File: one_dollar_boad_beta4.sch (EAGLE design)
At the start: 38 parts, among them IC1 ATTINY85, X1 USBPCB

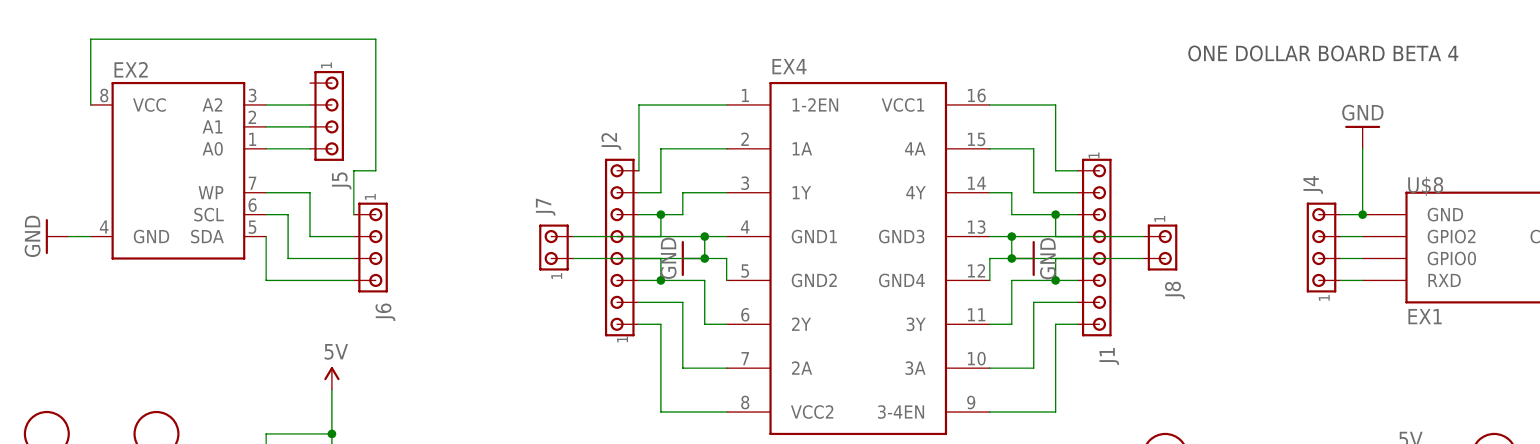
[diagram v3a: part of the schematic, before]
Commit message: GND retirado
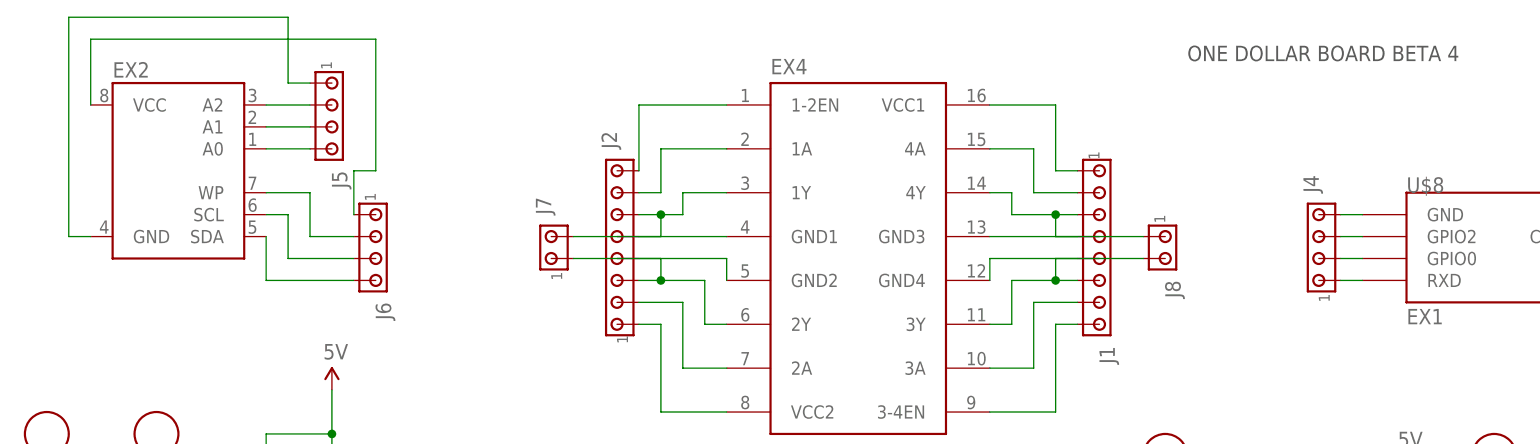
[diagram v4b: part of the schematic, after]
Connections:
- new net N$22: J4.4, U$8.GND
- new net N$49: EX4.GND2, J2.4
- new net N$50: EX4.GND1, J2.5
- new net N$51: EX4.GND4, J1.5
- new net N$52: EX4.GND3, J1.4
- new net N$53: EX2.GND, J5.1
- net GND: no longer EX2.GND, EX4.GND1, EX4.GND2, EX4.GND3, EX4.GND4, J1.4, J1.5, J2.4, J2.5, J4.4, U$8.GND
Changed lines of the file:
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@@
 <?xml version="1.0" encoding="utf-8"?>
 <!DOCTYPE eagle SYSTEM "eagle.dtd">
-<eagle version="6.6.0">
+<eagle version="7.5.0">
 <drawing>
 <settings>
@@
 <part name="J4" library="con-amp" deviceset="MTA04-100" device=""/>
 <part name="EX2" library="atmel" deviceset="AT24C*" device="P" value=""/>
-<part name="GND8" library="supply1" deviceset="GND" device=""/>
-<part name="GND9" library="SparkFun" deviceset="GND" device=""/>
-<part name="GND10" library="SparkFun" deviceset="GND" device=""/>
-<part name="GND11" library="SparkFun" deviceset="GND" device=""/>
 <part name="J5" library="con-amp" deviceset="MTA04-100" device=""/>
 <part name="J6" library="con-amp" deviceset="MTA04-100" device=""/>
@@
 <instance part="J4" gate="G$1" x="93.98" y="93.98" rot="R90"/>
 <instance part="EX2" gate="G$1" x="-38.1" y="104.14"/>
-<instance part="GND8" gate="1" x="-53.34" y="96.52" rot="R270"/>
-<instance part="GND9" gate="1" x="99.06" y="109.22" rot="R180"/>
-<instance part="GND10" gate="1" x="60.96" y="93.98" rot="R90"/>
-<instance part="GND11" gate="1" x="20.32" y="93.98" rot="R270"/>
 <instance part="J5" gate="G$1" x="-20.32" y="111.76" rot="R270"/>
 <instance part="J6" gate="G$1" x="-15.24" y="96.52" rot="R270"/>
@@
 </segment>
 <segment>
-<pinref part="EX2" gate="G$1" pin="GND"/>
-<pinref part="GND8" gate="1" pin="GND"/>
-<wire x1="-48.26" y1="96.52" x2="-50.8" y2="96.52" width="0.1524" layer="91"/>
-</segment>
-<segment>
-<pinref part="GND10" gate="1" pin="GND"/>
-<wire x1="58.42" y1="96.52" x2="58.42" y2="93.98" width="0.1524" layer="91"/>
-<pinref part="EX4" gate="G$1" pin="GND4"/>
-<wire x1="58.42" y1="93.98" x2="55.88" y2="93.98" width="0.1524" layer="91"/>
-<wire x1="55.88" y1="93.98" x2="55.88" y2="91.44" width="0.1524" layer="91"/>
-<pinref part="EX4" gate="G$1" pin="GND3"/>
-<wire x1="58.42" y1="96.52" x2="55.88" y2="96.52" width="0.1524" layer="91"/>
-<junction x="58.42" y="93.98"/>
-<pinref part="J1" gate="G$1" pin="4"/>
-<wire x1="66.04" y1="96.52" x2="58.42" y2="96.52" width="0.1524" layer="91"/>
-<pinref part="J1" gate="G$1" pin="5"/>
-<wire x1="66.04" y1="93.98" x2="58.42" y2="93.98" width="0.1524" layer="91"/>
-<junction x="58.42" y="96.52"/>
-</segment>
-<segment>
-<pinref part="EX4" gate="G$1" pin="GND1"/>
-<pinref part="GND11" gate="1" pin="GND"/>
-<wire x1="25.4" y1="96.52" x2="22.86" y2="96.52" width="0.1524" layer="91"/>
-<wire x1="22.86" y1="96.52" x2="22.86" y2="93.98" width="0.1524" layer="91"/>
-<pinref part="EX4" gate="G$1" pin="GND2"/>
-<wire x1="25.4" y1="91.44" x2="25.4" y2="93.98" width="0.1524" layer="91"/>
-<wire x1="25.4" y1="93.98" x2="22.86" y2="93.98" width="0.1524" layer="91"/>
-<junction x="22.86" y="93.98"/>
-<pinref part="J2" gate="G$1" pin="5"/>
-<wire x1="15.24" y1="96.52" x2="22.86" y2="96.52" width="0.1524" layer="91"/>
-<pinref part="J2" gate="G$1" pin="4"/>
-<wire x1="15.24" y1="93.98" x2="22.86" y2="93.98" width="0.1524" layer="91"/>
-<junction x="22.86" y="96.52"/>
-</segment>
-<segment>
-<pinref part="U$8" gate="G$1" pin="GND"/>
-<pinref part="GND9" gate="1" pin="GND"/>
-<wire x1="99.06" y1="99.06" x2="99.06" y2="106.68" width="0.1524" layer="91"/>
-<pinref part="J4" gate="G$1" pin="4"/>
-<wire x1="96.52" y1="99.06" x2="99.06" y2="99.06" width="0.1524" layer="91"/>
-<junction x="99.06" y="99.06"/>
-</segment>
-<segment>
 <pinref part="GND4" gate="1" pin="GND"/>
 <wire x1="116.84" y1="50.8" x2="116.84" y2="48.26" width="0.1524" layer="91"/>
@@
 </segment>
 </net>
+<net name="N$22" class="0">
+<segment>
+<pinref part="U$8" gate="G$1" pin="GND"/>
+<pinref part="J4" gate="G$1" pin="4"/>
+<wire x1="96.52" y1="99.06" x2="99.06" y2="99.06" width="0.1524" layer="91"/>
+</segment>
+</net>
+<net name="N$49" class="0">
+<segment>
+<pinref part="EX4" gate="G$1" pin="GND2"/>
+<wire x1="25.4" y1="91.44" x2="25.4" y2="93.98" width="0.1524" layer="91"/>
+<pinref part="J2" gate="G$1" pin="4"/>
+<wire x1="15.24" y1="93.98" x2="25.4" y2="93.98" width="0.1524" layer="91"/>
+</segment>
+</net>
+<net name="N$50" class="0">
+<segment>
+<pinref part="EX4" gate="G$1" pin="GND1"/>
+<pinref part="J2" gate="G$1" pin="5"/>
+<wire x1="15.24" y1="96.52" x2="25.4" y2="96.52" width="0.1524" layer="91"/>
+</segment>
+</net>
+<net name="N$51" class="0">
+<segment>
+<pinref part="EX4" gate="G$1" pin="GND4"/>
+<wire x1="55.88" y1="93.98" x2="55.88" y2="91.44" width="0.1524" layer="91"/>
+<pinref part="J1" gate="G$1" pin="5"/>
+<wire x1="66.04" y1="93.98" x2="55.88" y2="93.98" width="0.1524" layer="91"/>
+</segment>
+</net>
+<net name="N$52" class="0">
+<segment>
+<pinref part="EX4" gate="G$1" pin="GND3"/>
+<pinref part="J1" gate="G$1" pin="4"/>
+<wire x1="66.04" y1="96.52" x2="55.88" y2="96.52" width="0.1524" layer="91"/>
+</segment>
+</net>
+<net name="N$53" class="0">
+<segment>
+<pinref part="EX2" gate="G$1" pin="GND"/>
+<wire x1="-48.26" y1="96.52" x2="-50.8" y2="96.52" width="0.1524" layer="91"/>
+<wire x1="-50.8" y1="96.52" x2="-50.8" y2="121.92" width="0.1524" layer="91"/>
+<wire x1="-50.8" y1="121.92" x2="-25.4" y2="121.92" width="0.1524" layer="91"/>
+<wire x1="-25.4" y1="121.92" x2="-25.4" y2="114.3" width="0.1524" layer="91"/>
+<pinref part="J5" gate="G$1" pin="1"/>
+<wire x1="-25.4" y1="114.3" x2="-22.86" y2="114.3" width="0.1524" layer="91"/>
+</segment>
+</net>

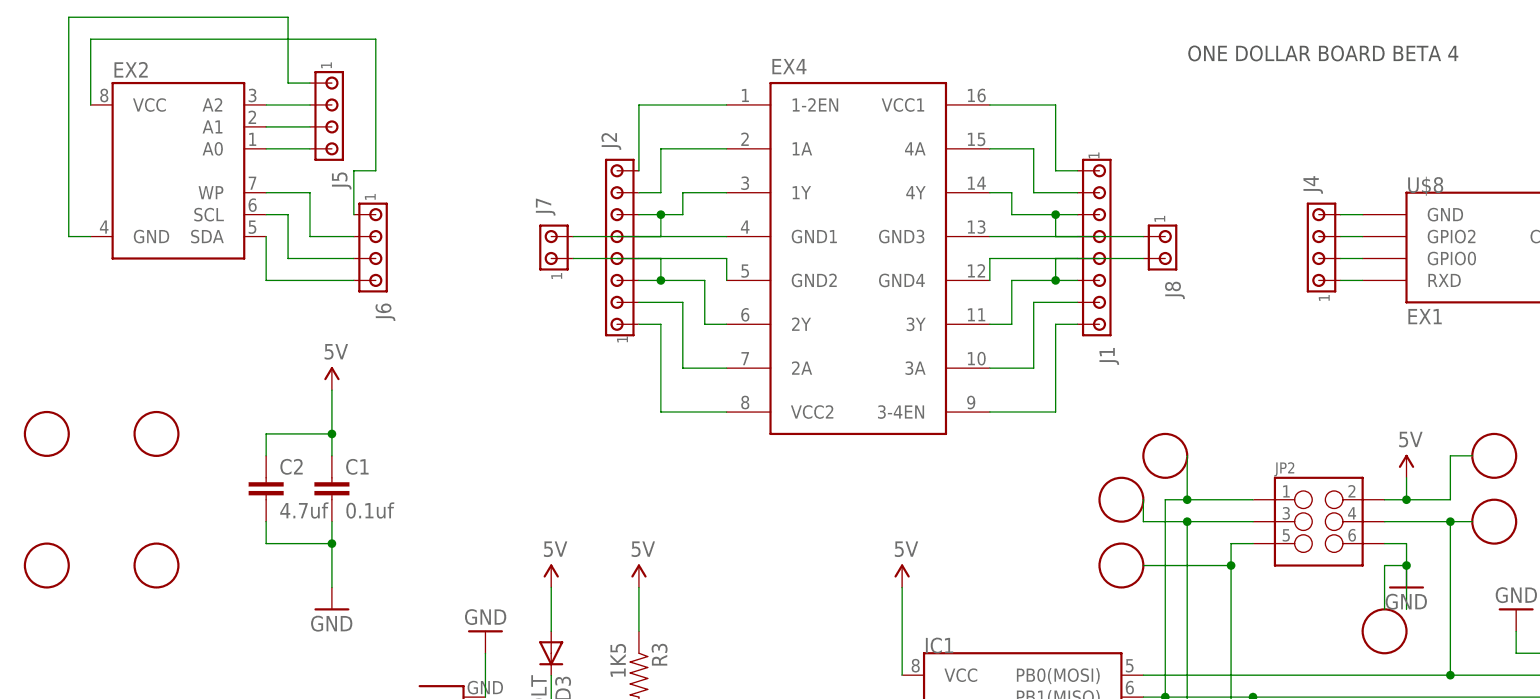
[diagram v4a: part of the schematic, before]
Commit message: Added files via upload
Adicionado alimentação externa
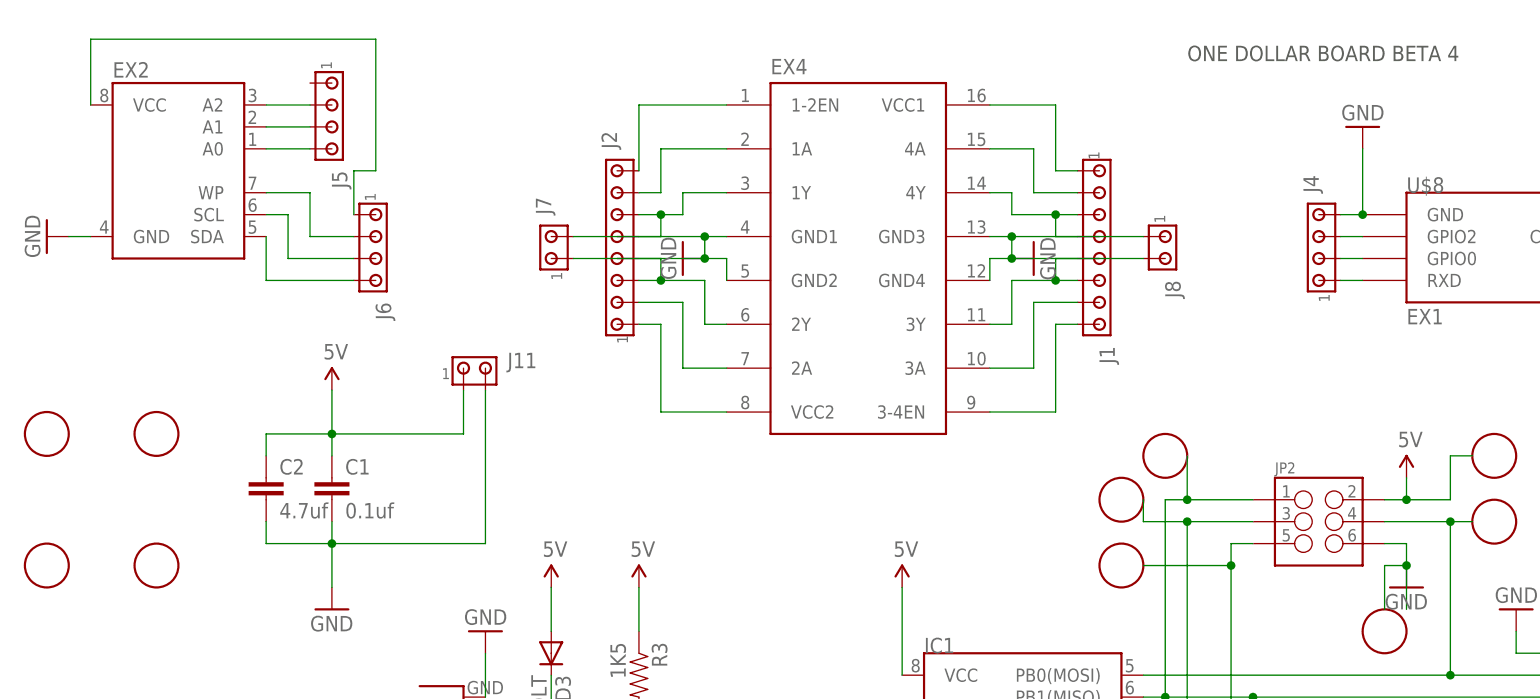
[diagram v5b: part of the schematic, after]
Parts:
- added J11: (no value), con-amp:MTA02-100
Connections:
- removed net N$22: J4.4, U$8.GND
- removed net N$49: EX4.GND2, J2.4
- removed net N$50: EX4.GND1, J2.5
- removed net N$51: EX4.GND4, J1.5
- removed net N$52: EX4.GND3, J1.4
- removed net N$53: EX2.GND, J5.1
- net 5V: now also J11.1
- net GND: now also EX2.GND, EX4.GND1, EX4.GND2, EX4.GND3, EX4.GND4, J1.4, J1.5, J11.2, J2.4, J2.5, J4.4, U$8.GND
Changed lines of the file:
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@@
 <?xml version="1.0" encoding="utf-8"?>
 <!DOCTYPE eagle SYSTEM "eagle.dtd">
-<eagle version="7.5.0">
+<eagle version="7.2.0">
 <drawing>
 <settings>
@@
 <part name="J4" library="con-amp" deviceset="MTA04-100" device=""/>
 <part name="EX2" library="atmel" deviceset="AT24C*" device="P" value=""/>
+<part name="GND8" library="supply1" deviceset="GND" device=""/>
+<part name="GND9" library="SparkFun" deviceset="GND" device=""/>
+<part name="GND10" library="SparkFun" deviceset="GND" device=""/>
+<part name="GND11" library="SparkFun" deviceset="GND" device=""/>
 <part name="J5" library="con-amp" deviceset="MTA04-100" device=""/>
 <part name="J6" library="con-amp" deviceset="MTA04-100" device=""/>
@@
 <part name="J9" library="con-amp" deviceset="MTA03-100" device=""/>
 <part name="J10" library="con-amp" deviceset="MTA03-100" device=""/>
+<part name="J11" library="con-amp" deviceset="MTA02-100" device=""/>
 </parts>
 <sheets>
@@
 <instance part="J4" gate="G$1" x="93.98" y="93.98" rot="R90"/>
 <instance part="EX2" gate="G$1" x="-38.1" y="104.14"/>
+<instance part="GND8" gate="1" x="-53.34" y="96.52" rot="R270"/>
+<instance part="GND9" gate="1" x="99.06" y="109.22" rot="R180"/>
+<instance part="GND10" gate="1" x="60.96" y="93.98" rot="R90"/>
+<instance part="GND11" gate="1" x="20.32" y="93.98" rot="R270"/>
 <instance part="J5" gate="G$1" x="-20.32" y="111.76" rot="R270"/>
 <instance part="J6" gate="G$1" x="-15.24" y="96.52" rot="R270"/>
@@
 <instance part="J9" gate="G$1" x="132.08" y="76.2"/>
 <instance part="J10" gate="G$1" x="132.08" y="68.58" rot="R180"/>
+<instance part="J11" gate="G$1" x="-5.08" y="81.28"/>
 </instances>
 <busses>
@@
 <wire x1="-27.94" y1="60.96" x2="-27.94" y2="63.5" width="0.1524" layer="91"/>
 <junction x="-20.32" y="60.96"/>
+<pinref part="J11" gate="G$1" pin="2"/>
+<wire x1="-2.54" y1="78.74" x2="-2.54" y2="60.96" width="0.1524" layer="91"/>
+<wire x1="-2.54" y1="60.96" x2="-20.32" y2="60.96" width="0.1524" layer="91"/>
 </segment>
 <segment>
@@
 <pinref part="GND7" gate="1" pin="GND"/>
 <wire x1="99.06" y1="5.08" x2="111.76" y2="5.08" width="0.1524" layer="91"/>
+</segment>
+<segment>
+<pinref part="EX2" gate="G$1" pin="GND"/>
+<pinref part="GND8" gate="1" pin="GND"/>
+<wire x1="-48.26" y1="96.52" x2="-50.8" y2="96.52" width="0.1524" layer="91"/>
+</segment>
+<segment>
+<pinref part="GND10" gate="1" pin="GND"/>
+<wire x1="58.42" y1="96.52" x2="58.42" y2="93.98" width="0.1524" layer="91"/>
+<pinref part="EX4" gate="G$1" pin="GND4"/>
+<wire x1="58.42" y1="93.98" x2="55.88" y2="93.98" width="0.1524" layer="91"/>
+<wire x1="55.88" y1="93.98" x2="55.88" y2="91.44" width="0.1524" layer="91"/>
+<pinref part="EX4" gate="G$1" pin="GND3"/>
+<wire x1="58.42" y1="96.52" x2="55.88" y2="96.52" width="0.1524" layer="91"/>
+<junction x="58.42" y="93.98"/>
+<pinref part="J1" gate="G$1" pin="4"/>
+<wire x1="66.04" y1="96.52" x2="58.42" y2="96.52" width="0.1524" layer="91"/>
+<pinref part="J1" gate="G$1" pin="5"/>
+<wire x1="66.04" y1="93.98" x2="58.42" y2="93.98" width="0.1524" layer="91"/>
+<junction x="58.42" y="96.52"/>
+</segment>
+<segment>
+<pinref part="EX4" gate="G$1" pin="GND1"/>
+<pinref part="GND11" gate="1" pin="GND"/>
+<wire x1="25.4" y1="96.52" x2="22.86" y2="96.52" width="0.1524" layer="91"/>
+<wire x1="22.86" y1="96.52" x2="22.86" y2="93.98" width="0.1524" layer="91"/>
+<pinref part="EX4" gate="G$1" pin="GND2"/>
+<wire x1="25.4" y1="91.44" x2="25.4" y2="93.98" width="0.1524" layer="91"/>
+<wire x1="25.4" y1="93.98" x2="22.86" y2="93.98" width="0.1524" layer="91"/>
+<junction x="22.86" y="93.98"/>
+<pinref part="J2" gate="G$1" pin="5"/>
+<wire x1="15.24" y1="96.52" x2="22.86" y2="96.52" width="0.1524" layer="91"/>
+<pinref part="J2" gate="G$1" pin="4"/>
+<wire x1="15.24" y1="93.98" x2="22.86" y2="93.98" width="0.1524" layer="91"/>
+<junction x="22.86" y="96.52"/>
+</segment>
+<segment>
+<pinref part="U$8" gate="G$1" pin="GND"/>
+<pinref part="GND9" gate="1" pin="GND"/>
+<wire x1="99.06" y1="99.06" x2="99.06" y2="106.68" width="0.1524" layer="91"/>
+<pinref part="J4" gate="G$1" pin="4"/>
+<wire x1="96.52" y1="99.06" x2="99.06" y2="99.06" width="0.1524" layer="91"/>
+<junction x="99.06" y="99.06"/>
 </segment>
 <segment>
@@
 <wire x1="-27.94" y1="73.66" x2="-20.32" y2="73.66" width="0.1524" layer="91"/>
 <junction x="-20.32" y="73.66"/>
+<pinref part="J11" gate="G$1" pin="1"/>
+<wire x1="-5.08" y1="78.74" x2="-5.08" y2="73.66" width="0.1524" layer="91"/>
+<wire x1="-5.08" y1="73.66" x2="-20.32" y2="73.66" width="0.1524" layer="91"/>
 </segment>
 <segment>
@@
 </segment>
 </net>
-<net name="N$22" class="0">
-<segment>
-<pinref part="U$8" gate="G$1" pin="GND"/>
-<pinref part="J4" gate="G$1" pin="4"/>
-<wire x1="96.52" y1="99.06" x2="99.06" y2="99.06" width="0.1524" layer="91"/>
-</segment>
-</net>
-<net name="N$49" class="0">
-<segment>
-<pinref part="EX4" gate="G$1" pin="GND2"/>
-<wire x1="25.4" y1="91.44" x2="25.4" y2="93.98" width="0.1524" layer="91"/>
-<pinref part="J2" gate="G$1" pin="4"/>
-<wire x1="15.24" y1="93.98" x2="25.4" y2="93.98" width="0.1524" layer="91"/>
-</segment>
-</net>
-<net name="N$50" class="0">
-<segment>
-<pinref part="EX4" gate="G$1" pin="GND1"/>
-<pinref part="J2" gate="G$1" pin="5"/>
-<wire x1="15.24" y1="96.52" x2="25.4" y2="96.52" width="0.1524" layer="91"/>
-</segment>
-</net>
-<net name="N$51" class="0">
-<segment>
-<pinref part="EX4" gate="G$1" pin="GND4"/>
-<wire x1="55.88" y1="93.98" x2="55.88" y2="91.44" width="0.1524" layer="91"/>
-<pinref part="J1" gate="G$1" pin="5"/>
-<wire x1="66.04" y1="93.98" x2="55.88" y2="93.98" width="0.1524" layer="91"/>
-</segment>
-</net>
-<net name="N$52" class="0">
-<segment>
-<pinref part="EX4" gate="G$1" pin="GND3"/>
-<pinref part="J1" gate="G$1" pin="4"/>
-<wire x1="66.04" y1="96.52" x2="55.88" y2="96.52" width="0.1524" layer="91"/>
-</segment>
-</net>
-<net name="N$53" class="0">
-<segment>
-<pinref part="EX2" gate="G$1" pin="GND"/>
-<wire x1="-48.26" y1="96.52" x2="-50.8" y2="96.52" width="0.1524" layer="91"/>
-<wire x1="-50.8" y1="96.52" x2="-50.8" y2="121.92" width="0.1524" layer="91"/>
-<wire x1="-50.8" y1="121.92" x2="-25.4" y2="121.92" width="0.1524" layer="91"/>
-<wire x1="-25.4" y1="121.92" x2="-25.4" y2="114.3" width="0.1524" layer="91"/>
-<pinref part="J5" gate="G$1" pin="1"/>
-<wire x1="-25.4" y1="114.3" x2="-22.86" y2="114.3" width="0.1524" layer="91"/>
-</segment>
-</net>
